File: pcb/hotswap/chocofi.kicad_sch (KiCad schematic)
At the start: 193 parts, among them J1 Conn_01x03, J2 Conn_01x04, J4 Conn_01x05, J5 Conn_01x05, J6 Conn_01x03, J7 Conn_01x03, J8 Conn_01x05-TPH-Thumbs, K2 FPC_8p_SPECIAL-thumbs-or-joys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, M1.6-1 MountingHoleM1.6, M1.6-10 MountingHoleM1.6, M1.6-11 MountingHoleM1.6, M1.6-12 MountingHoleM1.6, M1.6-13 MountingHoleM1.6, M1.6-14 MountingHoleM1.6, M1.6-15 MountingHoleM1.6, M1.6-16 MountingHoleM1.6, M1.6-17 MountingHoleM1.6, M1.6-18 MountingHoleM1.6, M1.6-19 MountingHoleM1.6, M1.6-2 MountingHoleM1.6, M1.6-20 MountingHoleM1.6, M1.6-21 MountingHoleM1.6, M1.6-22 MountingHoleM1.6, M1.6-23 MountingHoleM1.6, M1.6-24 MountingHoleM1.6, M1.6-25 MountingHoleM1.6, M1.6-26 MountingHoleM1.6, M1.6-27 MountingHoleM1.6, M1.6-28 MountingHoleM1.6, M1.6-3 MountingHoleM1.6, M1.6-4 MountingHoleM1.6, M1.6-5 MountingHoleM1.6, M1.6-6 MountingHoleM1.6, M1.6-7 MountingHoleM1.6, M1.6-8 MountingHoleM1.6, M1.6-9 MountingHoleM1.6, M2-1 MountingHoleM2, M2-2 MountingHoleM2, M2-3 Large_MountingHoleM3, M2-4 MountingHoleM2, M2-5 MountingHoleM2, M2-6 MountingHoleM2, M2-7 Large_MountingHoleM3, M2-8 Large_MountingHoleM3, M2-9 Large_MountingHoleM3, M2-hole2.1 MountingHoleM2, M2-hole2.5 MountingHoleM2, Q1 TIP120, Q2 IRLR7843TRPBF, SW1 SW_Chuk, SW10 SW_Chuk, SW11 SW_Chuk, SW12 SW_Chuk, SW13 SW_Chuk, SW14 SW_Chuk, SW15 SW_Chuk, SW16 SW_Chuk, SW17 SW_Chuk, SW18 SW_Chuk, SW2 SW_Chuk, SW22 Pull, SW23 Pull, SW24 Pull, SW3 SW_Chuk, SW4 SW_Chuk, SW5 SW_Chuk, SW6 SW_Chuk, SW7 SW_Chuk, SW8 SW_Chuk, SW9 SW_Chuk, T1 FPC_8pins_SPECIAL-thumbs, T2 FPC_8pins_SPECIAL-thumbs, T3 FPC_8pins_SPECIAL-thumbs, T4 FPC_8pins_SPECIAL-thumbs, U1 RP2040-ProMicro-with-18thgpio, U2 TRRS_Chuck, U3 RP2040-ProMicro-Chuk

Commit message: wip
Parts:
- M2-hole2: renamed from M2-hole2.5; footprint Switches_Chukozor:Mounting-hole-M2-hole2.5 -> Switches_Chukozor:Mounting-hole-M2
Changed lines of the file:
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@@
 		(dnp no)
 		(fields_autoplaced yes)
-		(property "Reference" "M2-hole2.5"
+		(property "Reference" "M2-hole2"
 			(at 293.37 387.6039 0)
 			(effects
@@
 			)
 		)
-		(property "Footprint" "Switches_Chukozor:Mounting-hole-M2-hole2.5"
+		(property "Footprint" "Switches_Chukozor:Mounting-hole-M2"
 			(at 290.322 388.874 0)
 			(effects
@@
 			(project "chocofi"
 				(path "/4976ae50-9ae0-4449-9f0b-b92cb3fc915b"
-					(reference "M2-hole2.5")
+					(reference "M2-hole2")
 					(unit 1)
 				)

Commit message: wip
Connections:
- net 3.3V-VIK: now also SLDR_Pads1.2 (3.3V); no longer SLDR_Pads1.1 (3.3V)
- net DR: now also SLDR_Pads1.6 (CHG/DIR/RDY); no longer SLDR_Pads1.5 (CHG/DIR/RDY)
- net GND: now also SLDR_Pads1.5 (GND); no longer SLDR_Pads1.4 (GND)
- net SCL: now also SLDR_Pads1.3 (SCL); no longer SLDR_Pads1.2 (SCL)
- net SDA: now also SLDR_Pads1.4 (SDA); no longer SLDR_Pads1.3 (SDA)
- net VBUS: now also SLDR_Pads1.1 (3.3V)
- net VIK_GP1: now also SLDR_Pads1.7 (CHG/DIR/RDY); no longer SLDR_Pads1.6 (CHG/DIR/RDY)
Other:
- moved on the sheet: JP2
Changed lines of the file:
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@@
 	(global_label "VBUS"
 		(shape input)
+		(at 408.686 348.996 180)
+		(effects
+			(font
+				(size 1.1938 1.1938)
+			)
+			(justify right)
+		)
+		(property "Intersheetrefs" "${INTERSHEET_REFS}"
+			(at 408.686 348.996 0)
+			(effects
+				(font
+					(size 1.27 1.27)
+				)
+				(hide yes)
+			)
+		)
+	)
+	(global_label "VBUS"
+		(shape input)
 		(at 139.446 321.564 180)
 		(fields_autoplaced yes)
@@
 	(global_label "5V-VIK"
 		(shape input)
-		(at 351.028 357.378 0)
+		(at 347.726 355.346 0)
 		(effects
 			(font
@@
 		)
 		(property "Intersheetrefs" "${INTERSHEET_REFS}"
-			(at 351.028 357.378 0)
+			(at 347.726 355.346 0)
 			(effects
 				(font
@@
 	(global_label "VBUS"
 		(shape input)
-		(at 343.408 357.378 180)
+		(at 340.106 355.346 180)
 		(fields_autoplaced yes)
 		(effects
@@
 		)
 		(property "Intersheetrefs" "${INTERSHEET_REFS}"
-			(at 335.9976 357.378 0)
+			(at 332.6956 355.346 0)
 			(effects
 				(font
@@
 		(pin "6"
 		)
+		(pin "7"
+		)
 		(instances
 			(project ""
@@
 	(symbol
 		(lib_id "Jumper:SolderJumper_2_Open")
-		(at 347.218 357.378 0)
+		(at 343.916 355.346 0)
 		(unit 1)
 		(exclude_from_sim no)
@@
 		(dnp no)
 		(property "Reference" "JP2"
-			(at 346.964 359.41 0)
+			(at 343.662 357.378 0)
 			(effects
 				(font
@@
 		)
 		(property "Value" "5V-VIK"
-			(at 344.932 354.838 0)
+			(at 341.63 352.806 0)
 			(effects
 				(font
@@
 		)
 		(property "Footprint" "Switches_Chukozor:SB-small"
-			(at 347.218 357.378 0)
+			(at 343.916 355.346 0)
 			(effects
 				(font
@@
 		)
 		(property "Datasheet" "~"
-			(at 347.218 357.378 0)
+			(at 343.916 355.346 0)
 			(effects
 				(font
@@
 		)
 		(property "Description" "Solder Jumper, 2-pole, open"
-			(at 347.218 357.378 0)
+			(at 343.916 355.346 0)
 			(effects
 				(font

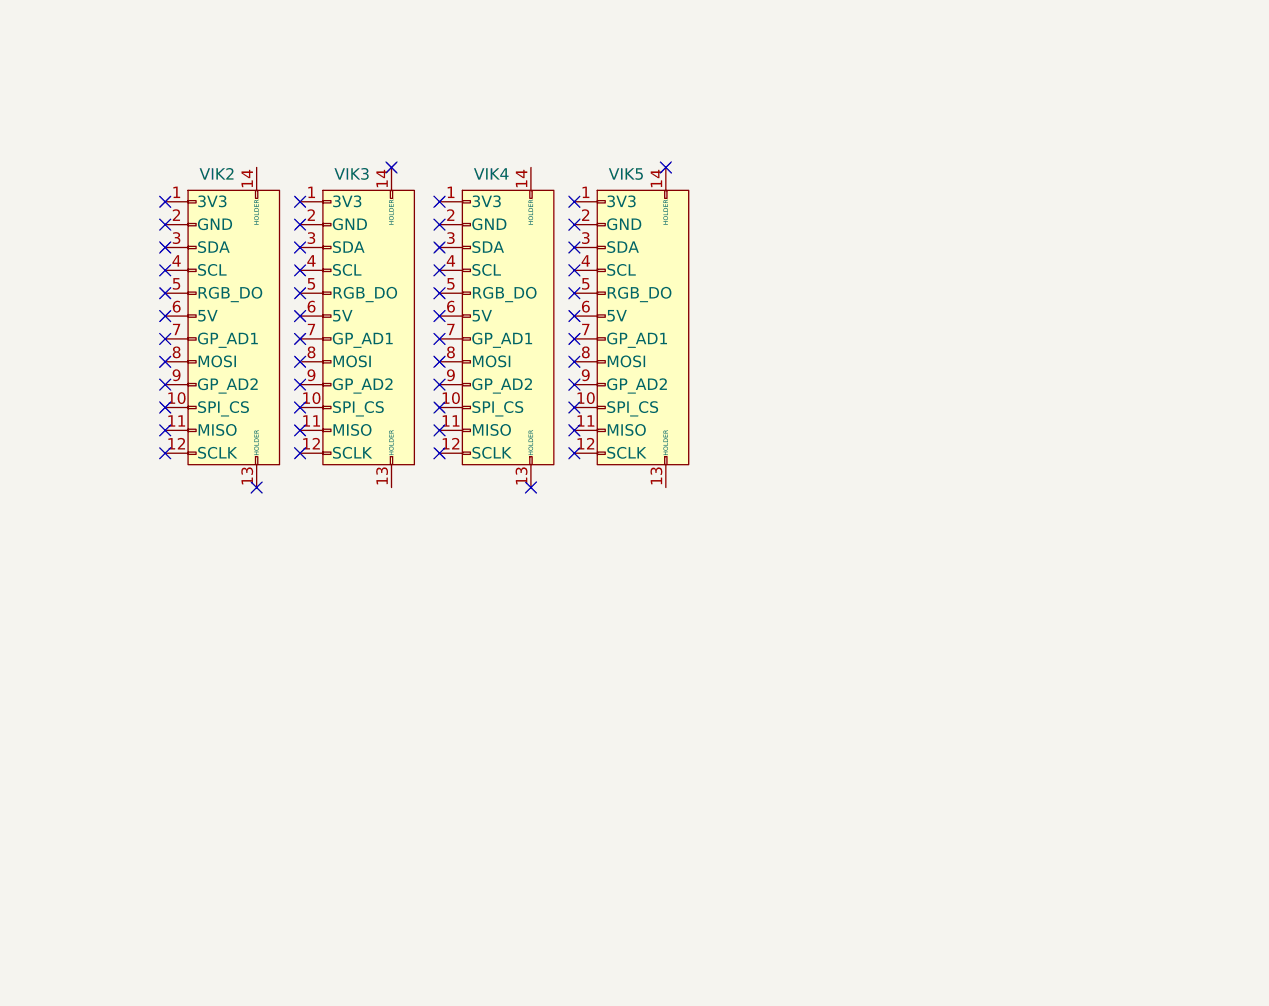
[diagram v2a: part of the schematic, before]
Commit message: add FPC connectors for stencil
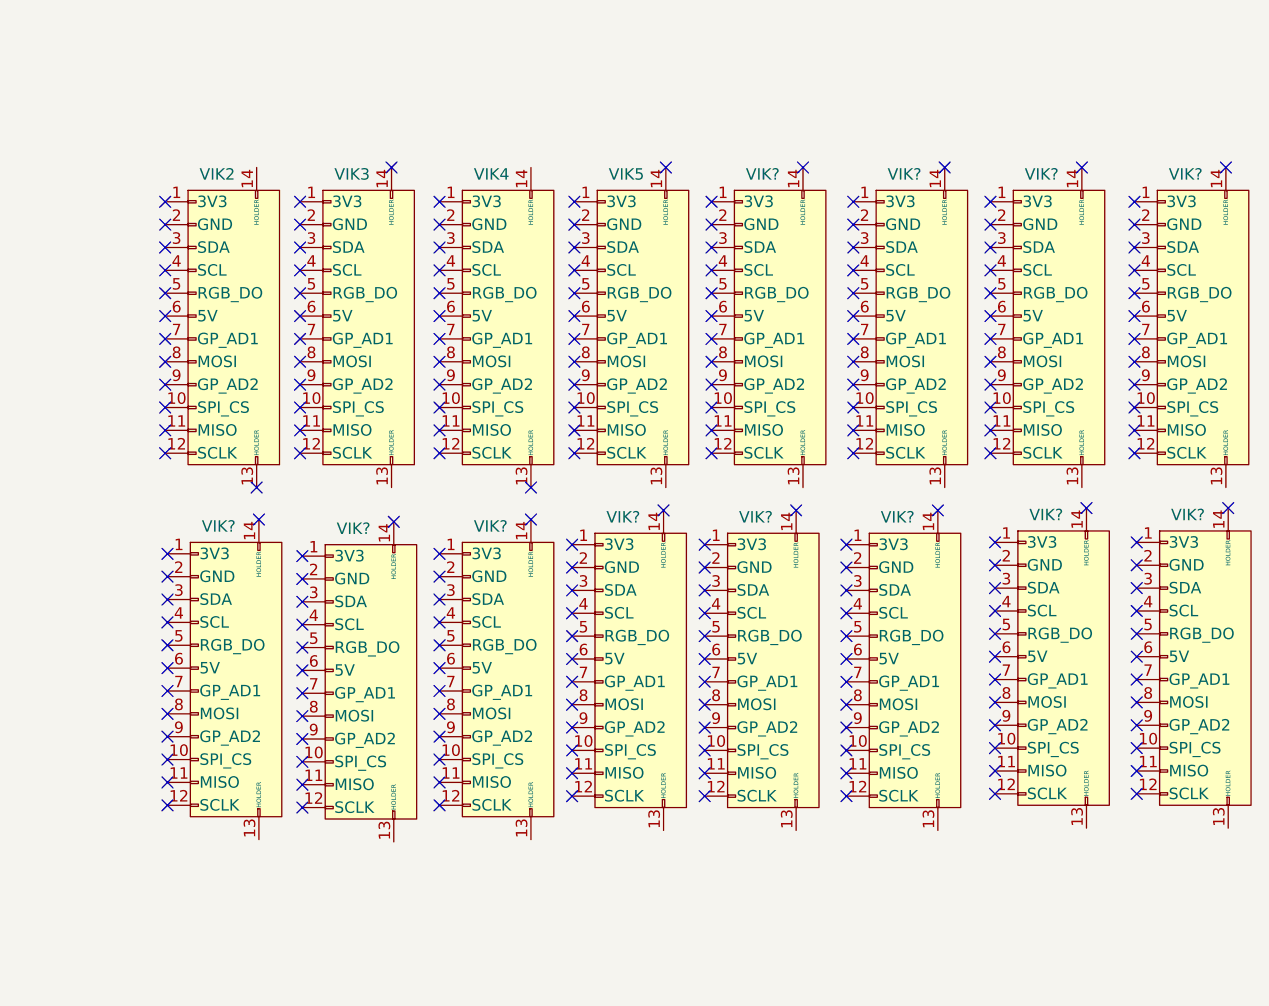
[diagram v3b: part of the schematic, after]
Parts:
- added VIK? (x12): ~, Switches_Chukozor:vik-keyboard-connector-horizontal-Both-Sides, symbol vik:vik-keyboard-connector
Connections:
- no-connect marks 81 -> 237

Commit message: wip (drawing of azoteq TPS65)
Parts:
- gave numbers to parts that had none: 12
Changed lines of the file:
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@@
 		(on_board yes)
 		(dnp no)
-		(property "Reference" "VIK?"
+		(property "Reference" "VIK12"
 			(at 729.488 291.846 0)
 			(effects
@@
 			(project "chocofi"
 				(path "/4976ae50-9ae0-4449-9f0b-b92cb3fc915b"
-					(reference "VIK?")
+					(reference "VIK12")
 					(unit 1)
 				)
@@
 		(on_board yes)
 		(dnp no)
-		(property "Reference" "VIK?"
+		(property "Reference" "VIK16"
 			(at 714.756 292.862 0)
 			(effects
@@
 			(project "chocofi"
 				(path "/4976ae50-9ae0-4449-9f0b-b92cb3fc915b"
-					(reference "VIK?")
+					(reference "VIK16")
 					(unit 1)
 				)
@@
 		(on_board yes)
 		(dnp no)
-		(property "Reference" "VIK?"
+		(property "Reference" "VIK13"
 			(at 744.22 291.846 0)
 			(effects
@@
 			(project "chocofi"
 				(path "/4976ae50-9ae0-4449-9f0b-b92cb3fc915b"
-					(reference "VIK?")
+					(reference "VIK13")
 					(unit 1)
 				)
@@
 		(on_board yes)
 		(dnp no)
-		(property "Reference" "VIK?"
+		(property "Reference" "VIK10"
 			(at 776.478 291.592 0)
 			(effects
@@
 			(project "chocofi"
 				(path "/4976ae50-9ae0-4449-9f0b-b92cb3fc915b"
-					(reference "VIK?")
+					(reference "VIK10")
 					(unit 1)
 				)
@@
 		(on_board yes)
 		(dnp no)
-		(property "Reference" "VIK?"
+		(property "Reference" "VIK15"
 			(at 684.53 292.862 0)
 			(effects
@@
 			(project "chocofi"
 				(path "/4976ae50-9ae0-4449-9f0b-b92cb3fc915b"
-					(reference "VIK?")
+					(reference "VIK15")
 					(unit 1)
 				)
@@
 		(on_board yes)
 		(dnp no)
-		(property "Reference" "VIK?"
+		(property "Reference" "VIK11"
 			(at 792.226 291.592 0)
 			(effects
@@
 			(project "chocofi"
 				(path "/4976ae50-9ae0-4449-9f0b-b92cb3fc915b"
-					(reference "VIK?")
+					(reference "VIK11")
 					(unit 1)
 				)
@@
 		(on_board yes)
 		(dnp no)
-		(property "Reference" "VIK?"
+		(property "Reference" "VIK7"
 			(at 760.73 253.746 0)
 			(effects
@@
 			(project "chocofi"
 				(path "/4976ae50-9ae0-4449-9f0b-b92cb3fc915b"
-					(reference "VIK?")
+					(reference "VIK7")
 					(unit 1)
 				)
@@
 		(on_board yes)
 		(dnp no)
-		(property "Reference" "VIK?"
+		(property "Reference" "VIK9"
 			(at 791.972 253.746 0)
 			(effects
@@
 			(project "chocofi"
 				(path "/4976ae50-9ae0-4449-9f0b-b92cb3fc915b"
-					(reference "VIK?")
+					(reference "VIK9")
 					(unit 1)
 				)
@@
 		(on_board yes)
 		(dnp no)
-		(property "Reference" "VIK?"
+		(property "Reference" "VIK6"
 			(at 744.982 253.746 0)
 			(effects
@@
 			(project "chocofi"
 				(path "/4976ae50-9ae0-4449-9f0b-b92cb3fc915b"
-					(reference "VIK?")
+					(reference "VIK6")
 					(unit 1)
 				)
@@
 		(on_board yes)
 		(dnp no)
-		(property "Reference" "VIK?"
+		(property "Reference" "VIK8"
 			(at 775.97 253.746 0)
 			(effects
@@
 			(project "chocofi"
 				(path "/4976ae50-9ae0-4449-9f0b-b92cb3fc915b"
-					(reference "VIK?")
+					(reference "VIK8")
 					(unit 1)
 				)
@@
 		(on_board yes)
 		(dnp no)
-		(property "Reference" "VIK?"
+		(property "Reference" "VIK17"
 			(at 699.516 293.116 0)
 			(effects
@@
 			(project "chocofi"
 				(path "/4976ae50-9ae0-4449-9f0b-b92cb3fc915b"
-					(reference "VIK?")
+					(reference "VIK17")
 					(unit 1)
 				)
@@
 		(on_board yes)
 		(dnp no)
-		(property "Reference" "VIK?"
+		(property "Reference" "VIK14"
 			(at 759.968 291.846 0)
 			(effects
@@
 			(project "chocofi"
 				(path "/4976ae50-9ae0-4449-9f0b-b92cb3fc915b"
-					(reference "VIK?")
+					(reference "VIK14")
 					(unit 1)
 				)

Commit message: wip
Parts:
- added M1.6-29: MountingHoleM1.6, Switches_Chukozor:Mounting-hole-M1.6, symbol Mechanical:MountingHole
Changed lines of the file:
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@@
+	)
+	(symbol
+		(lib_id "Mechanical:MountingHole")
+		(at 90.424 523.24 0)
+		(unit 1)
+		(exclude_from_sim no)
+		(in_bom no)
+		(on_board yes)
+		(dnp no)
+		(property "Reference" "M1.6-29"
+			(at 93.218 521.9699 0)
+			(effects
+				(font
+					(size 1.27 1.27)
+				)
+				(justify left)
+			)
+		)
+		(property "Value" "MountingHoleM1.6"
+			(at 93.218 524.5099 0)
+			(effects
+				(font
+					(size 1.27 1.27)
+				)
+				(justify left)
+			)
+		)
+		(property "Footprint" "Switches_Chukozor:Mounting-hole-M1.6"
+			(at 90.424 523.24 0)
+			(effects
+				(font
+					(size 1.27 1.27)
+				)
+				(hide yes)
+			)
+		)
+		(property "Datasheet" "~"
+			(at 90.424 523.24 0)
+			(effects
+				(font
+					(size 1.27 1.27)
+				)
+				(hide yes)
+			)
+		)
+		(property "Description" "Mounting Hole without connection"
+			(at 90.424 523.24 0)
+			(effects
+				(font
+					(size 1.27 1.27)
+				)
+				(hide yes)
+			)
+		)
+		(instances
+			(project "chocofi"
+				(path "/4976ae50-9ae0-4449-9f0b-b92cb3fc915b"
+					(reference "M1.6-29")
+					(unit 1)
+				)
+			)
+		)
 	)
 	(symbol

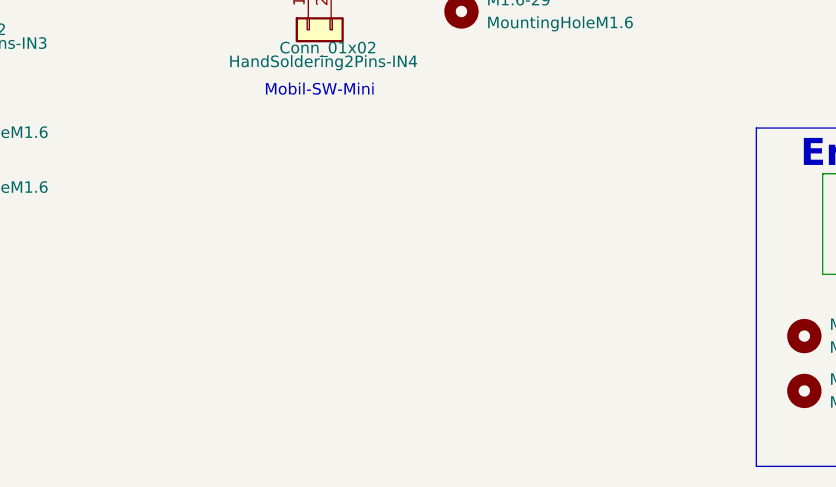
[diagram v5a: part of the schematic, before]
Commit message: add another mobil switch (MobilSW6) : smaller than the regular one.
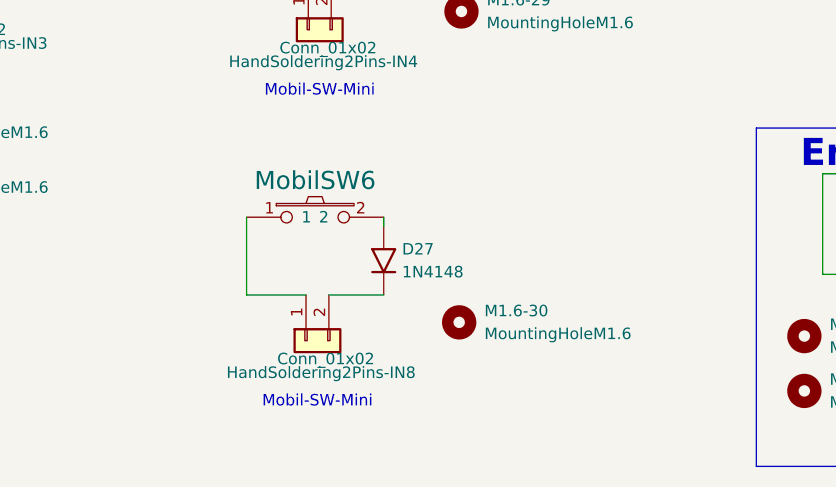
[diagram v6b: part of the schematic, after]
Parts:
- added D27: 1N4148, Switches_Chukozor:SMD_SOD_123_only_one_face, symbol Chukozor_symbols:1N4148
- added HandSoldering2Pins-IN8: Conn_01x02, Switches_Chukozor:HandSoldering-2pins-OUT-SMD, symbol Connector_Generic:Conn_01x02
- added M1.6-30: MountingHoleM1.6, Switches_Chukozor:Mounting-hole-M1.6, symbol Mechanical:MountingHole
- added MobilSW6: Pull, Switches_Chukozor:Kailh_socket_PG1350_reversible_Chukozor_-PULL-simplifiev2-TO-SOLDER, symbol Chukozor_symbols:SW_Chuk_-PULL_switches
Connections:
- new net: HandSoldering2Pins-IN8.1 (Pin_1), MobilSW6.1
- new net: D27.2 (A), MobilSW6.2
- new net: D27.1 (K), HandSoldering2Pins-IN8.2 (Pin_2)

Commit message: bidouille EC12
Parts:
- added ENC1, ENC5: RotaryEncoder_Switch, Switches_Chukozor:RotaryEncoder_Alps_EC12E-Switch_Vertical_H20mm, symbol Chukozor_symbols:EC12
- added J3, J9: Conn_01x03, Switches_Chukozor:EC12_ribon_connector, symbol Connector_Generic:Conn_01x03
- added M1.6-31, M1.6-32, M1.6-33, M1.6-34: MountingHoleM1.6, Switches_Chukozor:Mounting-hole-M1.6-withLarge2mm_Hole, symbol Mechanical:MountingHole
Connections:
- new net: ENC1.A, J3.1 (Pin_1)
- new net: ENC1.C, J3.2 (Pin_2)
- new net: ENC1.B, J3.3 (Pin_3)
- new net: ENC5.A, J9.1 (Pin_1)
- new net: ENC5.B, J9.3 (Pin_3)
- new net: ENC5.C, J9.2 (Pin_2)

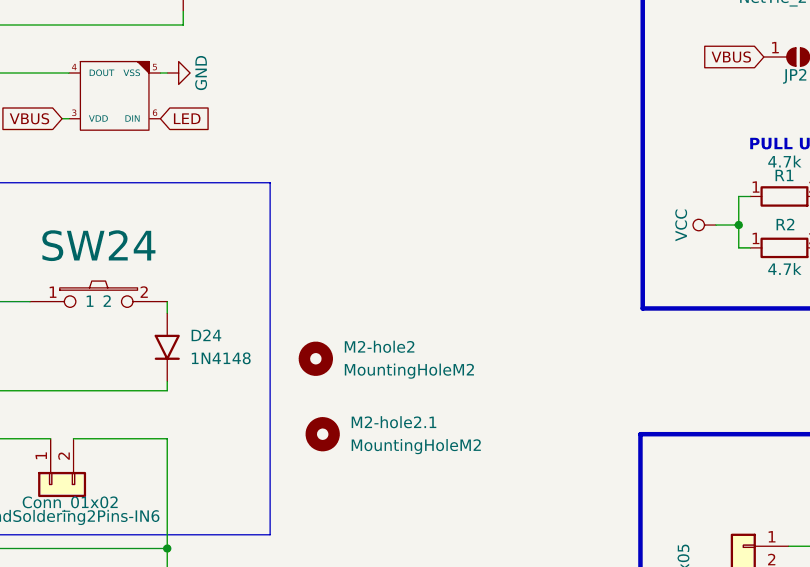
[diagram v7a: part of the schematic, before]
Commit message: add a hole and improve a bit tracks for encoder
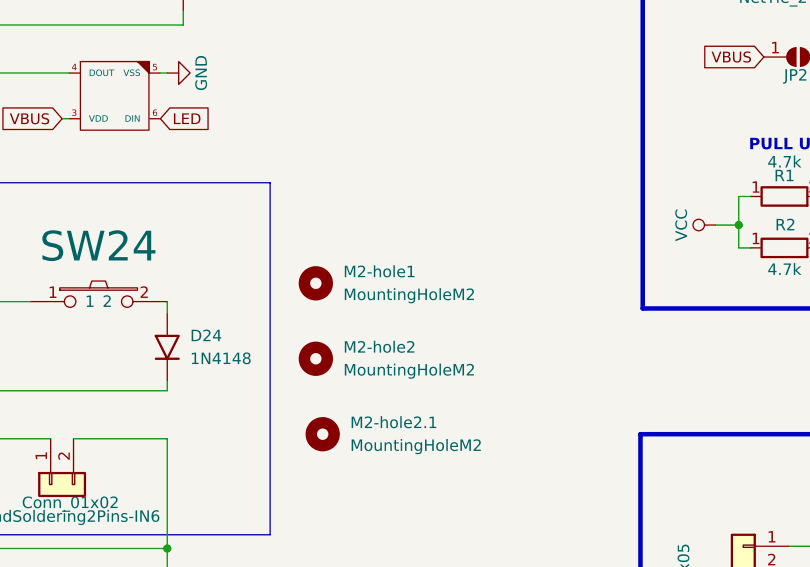
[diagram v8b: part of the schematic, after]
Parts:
- added M2-hole1: MountingHoleM2, Switches_Chukozor:Mounting-hole-M2, symbol Mechanical:MountingHole
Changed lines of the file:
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@@
+	)
+	(symbol
+		(lib_id "Mechanical:MountingHole")
+		(at 290.322 380.492 0)
+		(unit 1)
+		(exclude_from_sim no)
+		(in_bom no)
+		(on_board yes)
+		(dnp no)
+		(fields_autoplaced yes)
+		(property "Reference" "M2-hole1"
+			(at 293.37 379.2219 0)
+			(effects
+				(font
+					(size 1.27 1.27)
+				)
+				(justify left)
+			)
+		)
+		(property "Value" "MountingHoleM2"
+			(at 293.37 381.7619 0)
+			(effects
+				(font
+					(size 1.27 1.27)
+				)
+				(justify left)
+			)
+		)
+		(property "Footprint" "Switches_Chukozor:Mounting-hole-M2"
+			(at 290.322 380.492 0)
+			(effects
+				(font
+					(size 1.27 1.27)
+				)
+				(hide yes)
+			)
+		)
+		(property "Datasheet" "~"
+			(at 290.322 380.492 0)
+			(effects
+				(font
+					(size 1.27 1.27)
+				)
+				(hide yes)
+			)
+		)
+		(property "Description" "Mounting Hole without connection"
+			(at 290.322 380.492 0)
+			(effects
+				(font
+					(size 1.27 1.27)
+				)
+				(hide yes)
+			)
+		)
+		(instances
+			(project "chocofi"
+				(path "/4976ae50-9ae0-4449-9f0b-b92cb3fc915b"
+					(reference "M2-hole1")
+					(unit 1)
+				)
+			)
+		)
 	)
 	(symbol
